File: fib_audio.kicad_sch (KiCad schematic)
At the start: 0 parts

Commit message: added several ICs, implementted schematics for charger, boost converter and LDOs
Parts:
- added U4: WM8960CGEFL, Fibel2:QFN50P500X500X100-33N, symbol Fibel2:WM8960CGEFL
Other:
- note added: "2xMIC"
- note added: "2xSPEAKERS"
- note added: "AMP"
- note added: "JACK"
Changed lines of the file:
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@@
 	(generator_version "8.0")
 	(paper "A4")
+	(text "AMP"
+		(exclude_from_sim no)
+		(at 141.732 68.072 0)
+		(effects
+			(font
+				(size 1.27 1.27)
+			)
+		)
+	)
+	(text "JACK"
+		(exclude_from_sim no)
+		(at 141.732 57.658 0)
+		(effects
+			(font
+				(size 1.27 1.27)
+			)
+		)
+	)
+	(text "2xMIC"
+		(exclude_from_sim no)
+		(at 143.002 34.798 0)
+		(effects
+			(font
+				(size 1.27 1.27)
+			)
+		)
+	)
+	(text "2xSPEAKERS"
+		(exclude_from_sim no)
+		(at 145.542 46.482 0)
+		(effects
+			(font
+				(size 1.27 1.27)
+			)
+		)
+	)
+	(symbol
+		(lib_id "Fibel2:WM8960CGEFL")
+		(at 63.5 72.39 0)
+		(unit 1)
+		(exclude_from_sim no)
+		(in_bom yes)
+		(on_board yes)
+		(dnp no)
+		(fields_autoplaced yes)
+		(property "Reference" "U4"
+			(at 63.5 29.21 0)
+			(effects
+				(font
+					(size 1.27 1.27)
+				)
+			)
+		)
+		(property "Value" "WM8960CGEFL"
+			(at 63.5 31.75 0)
+			(effects
+				(font
+					(size 1.27 1.27)
+				)
+			)
+		)
+		(property "Footprint" "Fibel2:QFN50P500X500X100-33N"
+			(at 61.976 117.348 0)
+			(effects
+				(font
+					(size 1.27 1.27)
+				)
+				(justify bottom)
+				(hide yes)
+			)
+		)
+		(property "Datasheet" ""
+			(at 63.5 72.39 0)
+			(effects
+				(font
+					(size 1.27 1.27)
+				)
+				(hide yes)
+			)
+		)
+		(property "Description" ""
+			(at 63.5 72.39 0)
+			(effects
+				(font
+					(size 1.27 1.27)
+				)
+				(hide yes)
+			)
+		)
+		(property "MF" "Cirrus Logic Inc."
+			(at 53.594 119.38 0)
+			(effects
+				(font
+					(size 1.27 1.27)
+				)
+				(justify bottom)
+				(hide yes)
+			)
+		)
+		(property "MP" "WM8960CGEFL"
+			(at 52.578 115.062 0)
+			(effects
+				(font
+					(size 1.27 1.27)
+				)
+				(justify bottom)
+				(hide yes)
+			)
+		)
+		(pin "10"
+		)
+		(pin "11"
+		)
+		(pin "12"
+		)
+		(pin "13"
+		)
+		(pin "14"
+		)
+		(pin "15"
+		)
+		(pin "16"
+		)
+		(pin "17"
+		)
+		(pin "18"
+		)
+		(pin "19"
+		)
+		(pin "2"
+		)
+		(pin "20"
+		)
+		(pin "21"
+		)
+		(pin "22"
+		)
+		(pin "23"
+		)
+		(pin "24"
+		)
+		(pin "25"
+		)
+		(pin "26"
+		)
+		(pin "27"
+		)
+		(pin "28"
+		)
+		(pin "29"
+		)
+		(pin "3"
+		)
+		(pin "30"
+		)
+		(pin "31"
+		)
+		(pin "32"
+		)
+		(pin "33"
+		)
+		(pin "4"
+		)
+		(pin "5"
+		)
+		(pin "6"
+		)
+		(pin "7"
+		)
+		(pin "8"
+		)
+		(pin "9"
+		)
+		(pin "1"
+		)
+		(instances
+			(project "Fibel2"
+				(path "/862c21e2-7ec9-4f80-a33c-aad02ea9423e/17f77549-66cc-477f-9c69-749f4f7589f3"
+					(reference "U4")
+					(unit 1)
+				)
+			)
+		)
+	)
 )

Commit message: added symbol&footprint for orin/sodimm, added a bunch of specs and docs, partially implemented audio, full steam ahead
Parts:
- added C34, C40, C44, C52: 10uF, Untitled:C0603, symbol Untitled-eagle-import:CAP-0603
- added C35, C43, C45: 100nF, Untitled:C0402, symbol Untitled-eagle-import:CAP-0402
- added C36, C38, C49, C51: 33pF, Untitled:C0402, symbol Untitled-eagle-import:CAP-0402
- added C41, C42, C46, C48, C61, C62, C63: 100nF, Capacitor_SMD:C_0603_1608Metric, symbol Device:C_Small
- added C47, C50: 10uF, Capacitor_SMD:C_0603_1608Metric, symbol Device:C_Small
- added C54, C55: 100uF 10V, Untitled:C0805, symbol Untitled-eagle-import:CAP-0805
- added C56, C57, C58, C60: 100pF, Untitled:C0402, symbol Untitled-eagle-import:CAP-0402
- added C59: 680nF DNP, Untitled:C0402, symbol Untitled-eagle-import:CAP-0402
- added D4, D5: DF2S6.8FS, Untitled:SOD-923, symbol Untitled-eagle-import:D-ESD-2P'DF2S6.8FS'
- added J8: JST-2P, Untitled:HW2-SMD-2.0-90D, symbol Untitled-eagle-import:JST-2P-SMD'2.0'
- added J9: DNP AUDIO-JACK-8P-SMD, Untitled:AUDIO8P-SMD-3.5-14.5X6.1X4.0MM, symbol Untitled-eagle-import:AUDIO-JACK-8P-SMD'PJ-393'
- added K1: BUTTON-4PDTSM-62K-S-V-T/R(SN431), Untitled:SW4-SMD-6.0X6.0X5.0MM, symbol Untitled-eagle-import:BUTTON-4PDTSM-62K-S-V-T/R(SN431)
- added L3, L4: BLM18BD252SN1, Untitled:L0603, symbol Untitled-eagle-import:INDUCTOR/FERRITE-BEAD'0603'
- added L5, L6: 120R, Untitled:L0603, symbol Untitled-eagle-import:INDUCTOR/FERRITE-BEAD'0603'
- added L7, L8: MPZ1608D101BTA00, Untitled:L0603, symbol Untitled-eagle-import:INDUCTOR/FERRITE-BEAD'0603'
- added MIC1, MIC2: SAO-3729-M-42-008, Untitled:MIC4-SMD-3.76X2.95MM, symbol Untitled-eagle-import:MIC-MSM421A3729H8-C
- added PI1: RPI-ZERO, Untitled:RASPBERRYPI_BASTELSTUBE_V13_RASPI_BOARD_B+_FULL, symbol Untitled-eagle-import:RPI-ZERO
- added R13, R21, R22: 10k, Untitled:R0402, symbol Untitled-eagle-import:Discrete-new_RES-0402
- added R23, R24, R25, R26, R28: 10R, Resistor_SMD:R_0603_1608Metric, symbol Device:R_Small
- added R29, R30: 4.7K, Resistor_SMD:R_0603_1608Metric, symbol Device:R_Small
- added U7: WM8960, Untitled:QFN32G-0.5-5X5MM, symbol Untitled-eagle-import:AMPLIFIER-WM8960
- added X1: 24MHz 306020014, Untitled:OSC4-SMD-2.5X2.0X0.8MM, symbol Untitled-eagle-import:CRYSTAL-OSCILLATOR2.52.0
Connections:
- net MICBIAS: now reaches U4.1 (MICBIAS)
- net MICBIAS: now also C46.1, C47.1
- net D3V3: now reaches U4.10 (DBVDD)
- net D3V3: now also U4.8 (DCVDD), C61.1, C62.1, R29.1, R30.1
- net at U4.11 (MCLK): now also R23.1
- net at U4.12 (BCLK): now also R24.1
- net at U4.13 (DACLRC): now also U4.15 (ADCLRC/GPIO1), R25.1
- net at U4.14 (DACDAT): now also R28.1
- net at U4.16 (ADCDAT): now also R26.1
- net at U4.17 (SCLK): now also R29.2
- net at U4.18 (SDIN): now also R30.2
- net at U4.20 (SPKGND2): now also U4.24 (SPKGND1), U4.28 (AGND), U4.33 (EXP), U4.9 (DGND)
- net +5V: now reaches U4.21 (SPKVDD2)
- net +5V: now also U4.26 (SPKVDD1), C41.1, C42.1
- net VMID: now reaches U4.27 (VMID)
- net VMID: now also C48.1, C50.1, U7.27 (VMID)
- net A3V3: now reaches U4.32 (AVDD)
- net A3V3: now also C63.1
- new net: C51.2, C52.1, L4.2
- new net: C55.1, U7.31 (HP_L)
- new net: C49.2, L4.1, MIC2.4 (OUT)
- new net: J9.3, L7.2
- new net: J9.4, L8.2
- new net: C54.1, U7.29 (HP_R)
- new net: L6.1, U7.19 (SPK_RN)
- new net: C56.2, C59.2, J8.+ (1), L6.2
- new net: C36.2, L3.1, MIC1.4 (OUT)
- new net: L5.1, U7.22 (SPK_RP)
- new net: C57.2, C59.1, J8.- (2), L5.2
- new net: C38.2, C40.1, L3.2
- new net 3V3: PI1.1 (3V3@1)
- new net AVDD_3V3: C34.2, C35.2, C44.2, C45.2, MIC1.1 (VDD), MIC2.1 (VDD)
- new net GND: C34.1, C35.1, C36.1, C38.1, C41.2, C42.2, C43.1, C44.1, C45.1, C46.2, C47.2, C48.2, C49.1, C50.2, C51.1, C56.1, C57.1, C58.1, C60.1, C61.2, C62.2, C63.2, D4.2 (1), D5.2 (1), J8.3, J8.4, J9.1, J9.2, J9.5, J9.6, K1.2 (B0), K1.3 (B1), MIC1.2 (GND), MIC1.3 (GND@1), MIC2.2 (GND), MIC2.3 (GND@1), PI1.14 (GND@4), PI1.20 (GND@5), PI1.25 (GND@2), PI1.30 (GND@6), PI1.34 (GND@7), PI1.39 (GND@3), PI1.6 (GND@8), PI1.9 (GND@1), R21.1, R22.1, X1.2 (GND)
- new net GPIO12: PI1.32 (GPIO12)
- new net GPIO13: PI1.33 (GPIO13)
- new net GPIO17: K1.1 (A0), K1.4 (A1), R13.1
- new net HP_L: C55.2, C58.2, D4.1 (2), L8.1, R21.2
- new net HP_R: C54.2, C60.2, D5.1 (2), L7.1, R22.2
- new net I2C_SCL: PI1.5 (GPIO3/SCL1)
- new net I2C_SDA: PI1.3 (GPIO2/SDA1)
- new net I2S_ADC: PI1.38 (GPIO20), R26.2
- new net I2S_CLK: PI1.12 (GPIO18), R24.2
- new net I2S_DAC: PI1.40 (GPIO21), R28.2
- new net I2S_LRCLK: PI1.35 (GPIO19), R25.2
- new net LINPUT1: C52.2
- new net MCLK: R23.2, X1.3 (OUT)
- new net RINPUT1: C40.2
- new net UART_RXD0: PI1.10 (RXD0/GPIO15)
- new net UART_TXD0: PI1.8 (TXD0/GPIO14)
- new net VDD_3V3: C43.2, PI1.17 (3V3@2), R13.2, X1.1 (ENABLE), X1.4 (VDD)
- new net VDD_5V: PI1.2 (5V0@1), PI1.4 (5V0@2)
- no-connect marks 0 -> 3
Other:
- note removed: "2xMIC"
- note removed: "2xSPEAKERS"
- note removed: "AMP"
- note removed: "JACK"
- moved on the sheet: U4

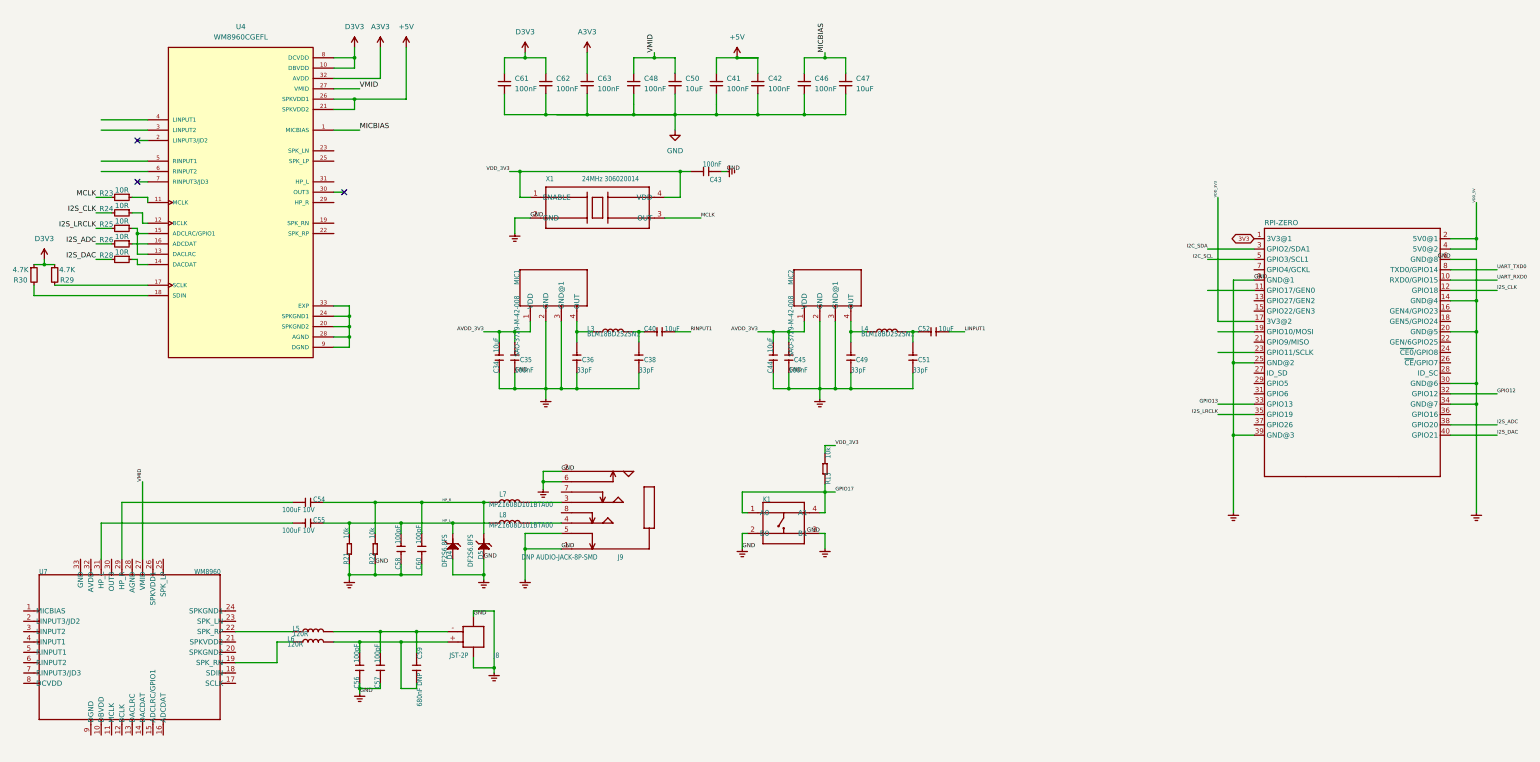
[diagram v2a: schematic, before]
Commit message: added usb+PD+DP & pcie implementations from antmicro design, added specs for USB components, rethought power+usb arch
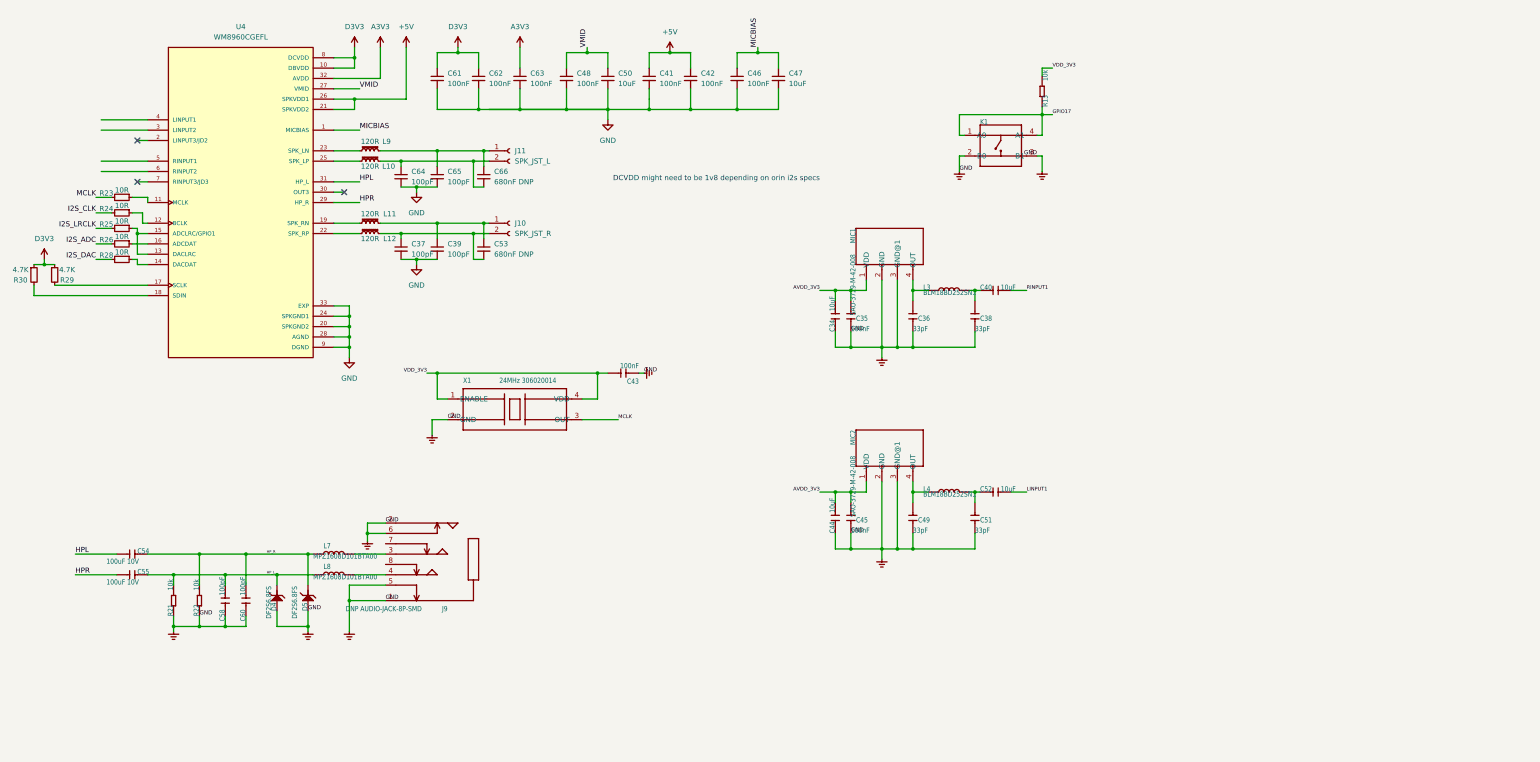
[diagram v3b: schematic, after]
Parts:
- removed C56, C57: 100pF, Untitled:C0402, symbol Untitled-eagle-import:CAP-0402
- removed C59: 680nF DNP, Untitled:C0402, symbol Untitled-eagle-import:CAP-0402
- removed J8: JST-2P, Untitled:HW2-SMD-2.0-90D, symbol Untitled-eagle-import:JST-2P-SMD'2.0'
- removed L5, L6: 120R, Untitled:L0603, symbol Untitled-eagle-import:INDUCTOR/FERRITE-BEAD'0603'
- removed PI1: RPI-ZERO, Untitled:RASPBERRYPI_BASTELSTUBE_V13_RASPI_BOARD_B+_FULL, symbol Untitled-eagle-import:RPI-ZERO
- removed U7: WM8960, Untitled:QFN32G-0.5-5X5MM, symbol Untitled-eagle-import:AMPLIFIER-WM8960
- added C37, C39, C64, C65: 100pF, Capacitor_SMD:C_0603_1608Metric, symbol Device:C_Small
- added C53, C66: 680nF DNP, Capacitor_SMD:C_0603_1608Metric, symbol Device:C_Small
- added J10: SPK_JST_R, symbol Connector:Conn_01x02_Socket
- added J11: SPK_JST_L, symbol Connector:Conn_01x02_Socket
- added L10, L11, L12, L9: 120R, symbol Device:L_Ferrite_Small
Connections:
- net GND: now also U4.20 (SPKGND2), U4.24 (SPKGND1), U4.28 (AGND), U4.33 (EXP), U4.9 (DGND), C37.2, C39.2, C64.2, C65.2
- net HPR: now reaches C55.1
- net HPR: now also U4.29 (HP_R)
- net at U4.19 (SPK_RN): now also L11.1
- net at U4.22 (SPK_RP): now also L12.1
- net at U4.23 (SPK_LN): now also L9.1
- net at U4.25 (SPK_LP): now also L10.1
- net HPL: now reaches U4.31 (HP_L)
- net HPL: now also C54.1
- new net: C39.1, C53.1, J10.1 (Pin_1), L11.2
- new net: C37.1, C53.2, J10.2 (Pin_2), L12.2
- new net: C64.1, C66.2, J11.2 (Pin_2), L10.2
- new net: C65.1, C66.1, J11.1 (Pin_1), L9.2
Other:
- note added: "DCVDD might need to be 1v8 depending on orin i2s specs"
- moved on the sheet: C34, C35, C36, C38, C40, C41, C42, C43, C44, C45, C46, C47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

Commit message: added nets for 40 pin headers (epd & rpi header) connected some of the nets i'm reeusing
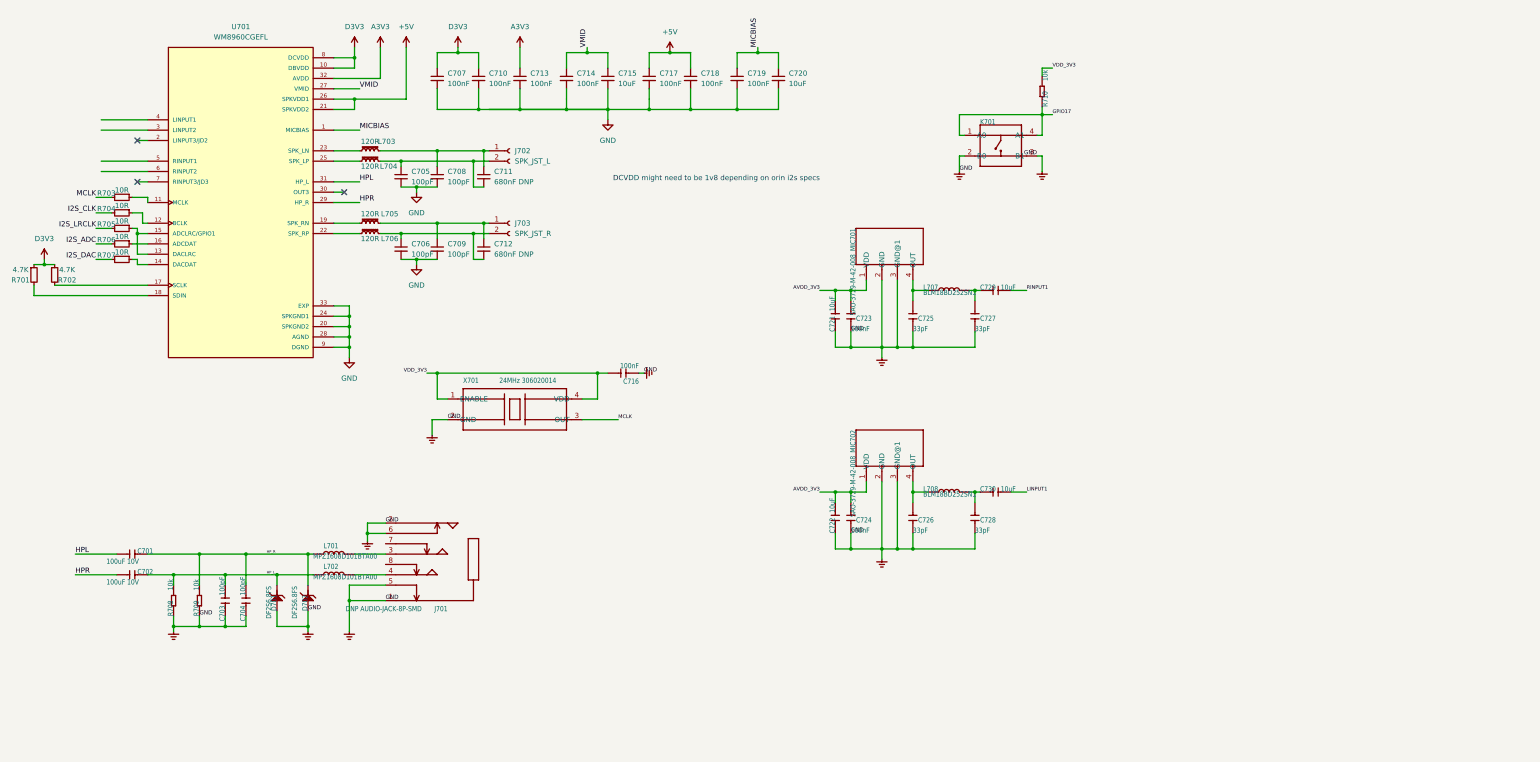
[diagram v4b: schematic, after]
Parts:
- C701: renamed from C54; footprint Untitled:C0805 -> Capacitor_SMD:C_0805_2012Metric
- C702: renamed from C55; footprint Untitled:C0805 -> Capacitor_SMD:C_0805_2012Metric
- C703: renamed from C58; footprint Untitled:C0402 -> Capacitor_SMD:C_0603_1608Metric
- C704: renamed from C60; footprint Untitled:C0402 -> Capacitor_SMD:C_0603_1608Metric
- C716: renamed from C43; footprint Untitled:C0402 -> Capacitor_SMD:C_0603_1608Metric
- C721: renamed from C34; footprint Untitled:C0603 -> Capacitor_SMD:C_0603_1608Metric
- C722: renamed from C44; footprint Untitled:C0603 -> Capacitor_SMD:C_0603_1608Metric
- C723: renamed from C35; footprint Untitled:C0402 -> Capacitor_SMD:C_0603_1608Metric
- C724: renamed from C45; footprint Untitled:C0402 -> Capacitor_SMD:C_0603_1608Metric
- C725: renamed from C36; footprint Untitled:C0402 -> Capacitor_SMD:C_0603_1608Metric
- C726: renamed from C49; footprint Untitled:C0402 -> Capacitor_SMD:C_0603_1608Metric
- C727: renamed from C38; footprint Untitled:C0402 -> Capacitor_SMD:C_0603_1608Metric
- C728: renamed from C51; footprint Untitled:C0402 -> Capacitor_SMD:C_0603_1608Metric
- C729: renamed from C40; footprint Untitled:C0603 -> Capacitor_SMD:C_0603_1608Metric
- C730: renamed from C52; footprint Untitled:C0603 -> Capacitor_SMD:C_0603_1608Metric
- J702: renamed from J11; footprint (none) -> Capacitor_SMD:C_0603_1608Metric
- J703: renamed from J10; footprint (none) -> Capacitor_SMD:C_0603_1608Metric
- R708: renamed from R21; footprint Untitled:R0402 -> Resistor_SMD:R_0603_1608Metric
- R709: renamed from R22; footprint Untitled:R0402 -> Resistor_SMD:R_0603_1608Metric
- R710: renamed from R13; footprint Untitled:R0402 -> Resistor_SMD:R_0603_1608Metric
- renumbered C64 to C705, C37 to C706, C61 to C707, C65 to C708, C39 to C709, C62 to C710, C66 to C711, C53 to C712, C63 to C713, C48 to C714, C50 to C715, C41 to C717, C42 to C718, C46 to C719, C47 to C720, D4 to D701, D5 to D702, J9 to J701, K1 to K701, L7 to L701, L8 to L702, L9 to L703, L10 to L704, L11 to L705, L12 to L706, L3 to L707, L4 to L708, MIC1 to MIC701, MIC2 to MIC702, R30 to R701, R29 to R702, R23 to R703, R24 to R704, R25 to R705, R26 to R706, R28 to R707, U4 to U701, X1 to X701
